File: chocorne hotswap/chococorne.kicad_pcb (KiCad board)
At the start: 2 copper layers, 261.7 x 87.7 mm, 108 parts, among them J1 MJ-4PP-9, J2 OLED, SW1 SW_PUSH, SW10 SW_PUSH, SW11 SW_PUSH, SW12 SW_PUSH, SW13 SW_PUSH, SW14 SW_PUSH, SW15 SW_PUSH, SW16 SW_PUSH, SW17 SW_PUSH, SW18 SW_PUSH, SW19 SW_PUSH, SW2 SW_PUSH, SW20 SW_PUSH, SW21 SW_PUSH, SW3 SW_PUSH, SW4 SW_PUSH, SW5 SW_PUSH, SW6 SW_PUSH, SW7 SW_PUSH, SW8 SW_PUSH, SW9 SW_PUSH, U1 ProMicro

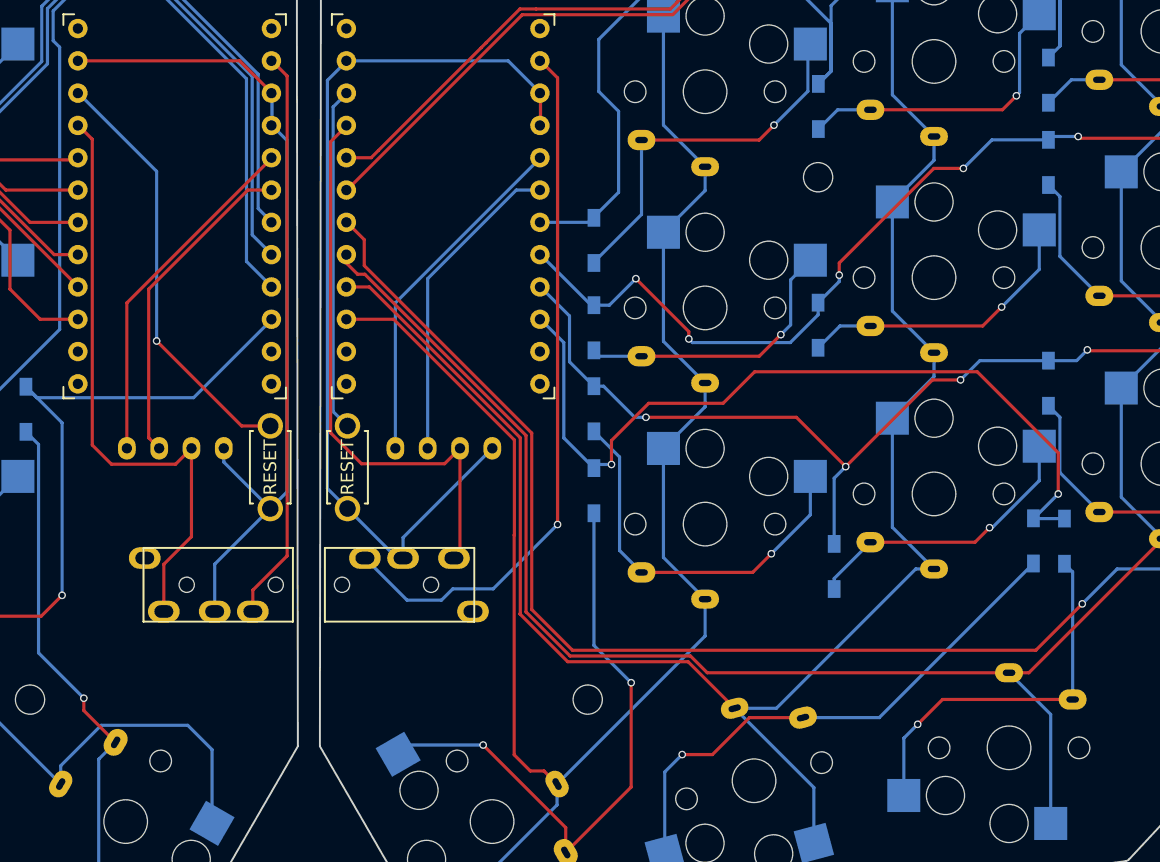
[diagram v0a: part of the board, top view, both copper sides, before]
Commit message: chocorne: add oled cover m2 holes
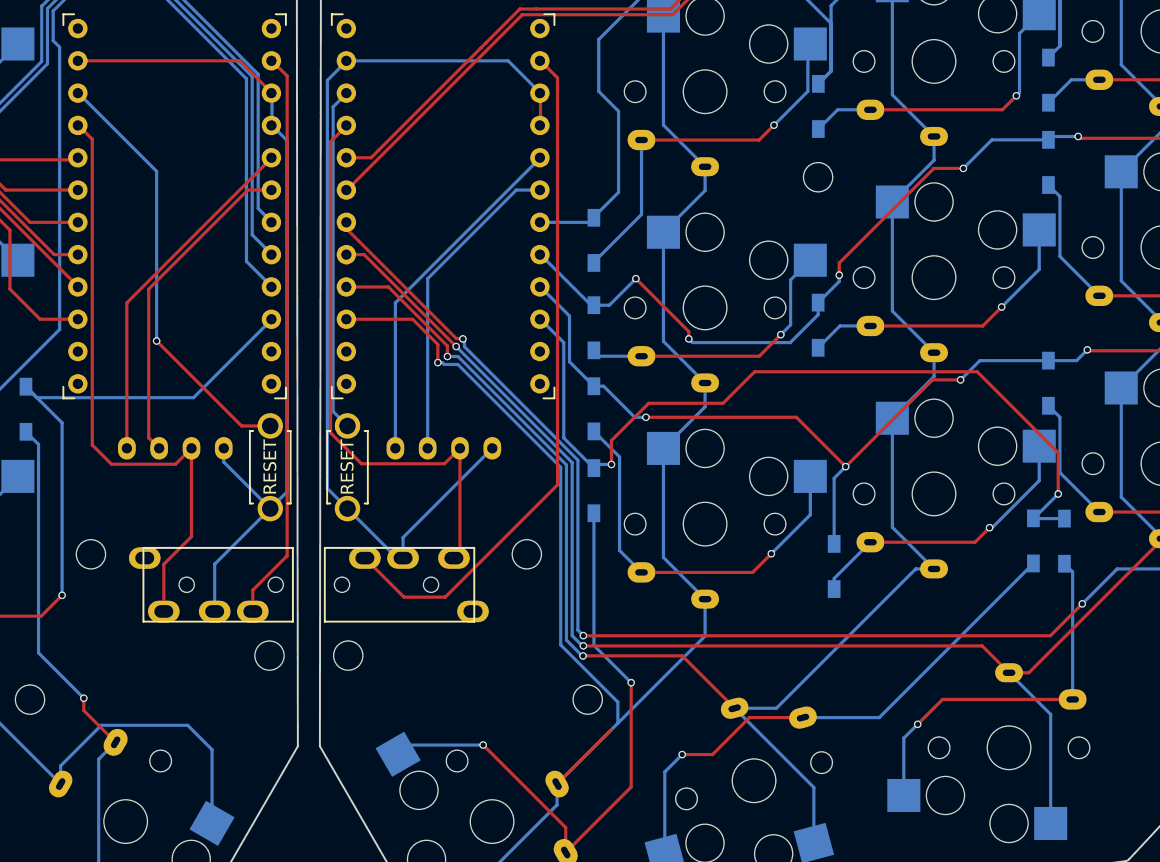
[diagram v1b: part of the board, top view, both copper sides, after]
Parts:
- added h2: h2, holykeebs:M2_HOLE_NPH, B.Cu at (164.8, 102.3)
- added h2: h2, holykeebs:M2_HOLE_NPH, F.Cu at (130.5, 102.3)
- added h2: h2, holykeebs:M2_HOLE_NPH, F.Cu at (144.6, 110.3)
- added h2: h2, holykeebs:M2_HOLE_NPH, B.Cu at (150.8, 110.3)
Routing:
- net col5: track 246.9 -> 251.3 mm, vias 4 -> 5
- net data: track 100.9 -> 98.9 mm, vias 1 -> 0
- net col2: track 320.0 -> 318.2 mm, vias 1 -> 3
- net col3: track 328.2 -> 328.8 mm, vias 0 -> 2
- net col4: track 281.8 -> 282.3 mm, vias 0 -> 2
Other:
- board text added: "5c02c88"
- board text removed: "427d1a3"

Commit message: chocorne: bump version
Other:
- board text added: "52d4260"
- board text removed: "5c02c88"
